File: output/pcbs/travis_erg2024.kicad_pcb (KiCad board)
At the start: 2 copper layers, 406.4 x 146.4 mm, 193 parts

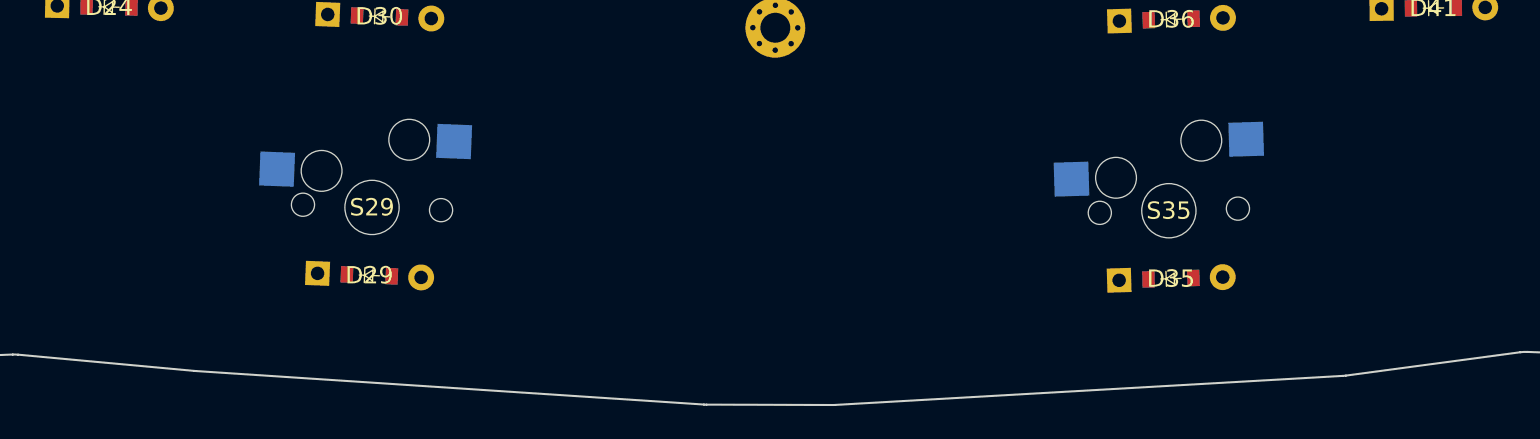
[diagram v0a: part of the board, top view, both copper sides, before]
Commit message: added stabs
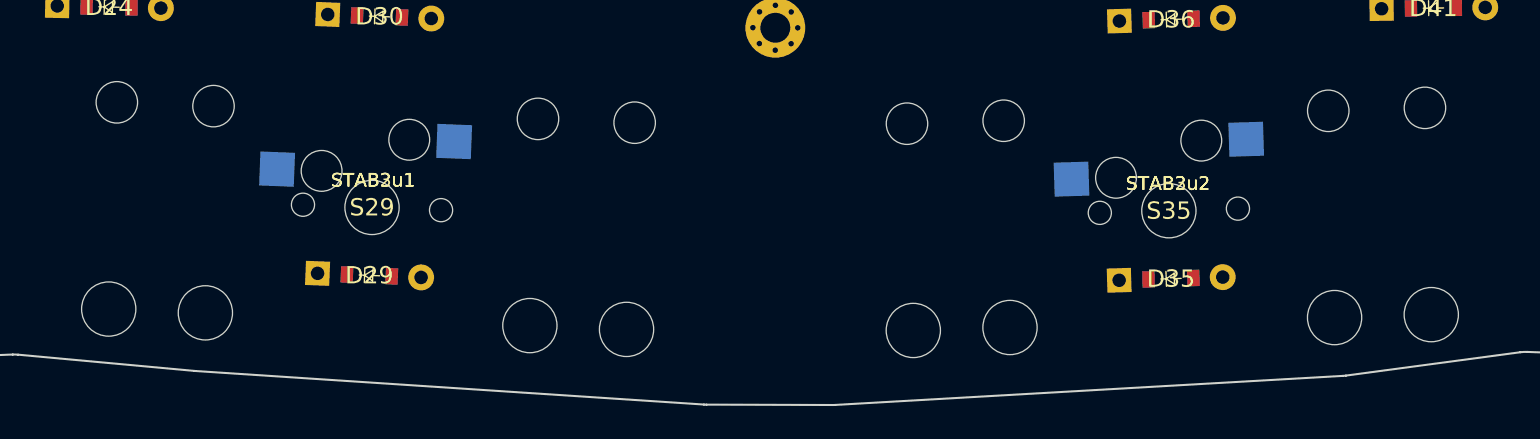
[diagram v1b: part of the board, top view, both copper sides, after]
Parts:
- added STAB2u1: Stabilizer_MX_2.00u, Stabilizer_MX_2.00u, F.Cu at (134.1, 169.9)
- added STAB2u2: Stabilizer_MX_2.00u, Stabilizer_MX_2.00u, F.Cu at (192.7, 170.1)
- added STAB3u1: Stabilizer_MX_3.00u, Stabilizer_MX_3.00u, F.Cu at (134.1, 169.9)
- added STAB3u2: Stabilizer_MX_3.00u, Stabilizer_MX_3.00u, F.Cu at (192.7, 170.1)
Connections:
- DIP1 pad 1: mux0 -> (no net)
- DIP1 pad 10: col5 -> (no net)
- DIP1 pad 11: col4 -> (no net)
- DIP1 pad 12: col3 -> (no net)
- DIP1 pad 13: col2 -> (no net)
- DIP1 pad 14: col1 -> (no net)
- DIP1 pad 15: col0 -> (no net)
- DIP1 pad 2: mux1 -> (no net)
- DIP1 pad 3: mux2 -> (no net)
- DIP1 pad 5: mux3 -> (no net)
- DIP1 pad 7: col7 -> (no net)
- DIP1 pad 9: col6 -> (no net)
- REF** pad D: (no net) -> undefined
- REF** pad S1: GND -> (no net)
- REF** pad S2: GND -> (no net)
- ROT1 pad 1: GND -> (no net)
- ROT1 pad 2: GND -> (no net)

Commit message: try alt stab
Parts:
- STAB2u2: value Stabilizer_MX_2.00u -> MX_Stabilizer_Cutout-2u; footprint Stabilizer_MX_2.00u -> MX_Stabilizer_Cutout-2u
- turned STAB2u1 to 177.75 degrees

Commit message: 3d adjustments
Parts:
- STAB2u2: value MX_Stabilizer_Cutout-2u -> Stabilizer_MX_2.00u; footprint MX_Stabilizer_Cutout-2u -> Stabilizer_MX_2.00u
- turned STAB2u2 to 181.75 degrees
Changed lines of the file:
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@@
     )
   )
-    (module MX_Stabilizer_Cutout-2u (layer F.Cu)
-    (at 192.703245 170.1296884 1.75)
-    (fp_text reference "STAB2u2" (at 0.25 10.05) (layer Eco2.User) hide hide
+    (module Stabilizer_MX_2.00u (layer F.Cu)
+    (descr "MX PCB Stabilizer 2.00u 2.25u 2.50u 2.75u")
+    (tags "MX Keyboard Stabilizer 2.00u 2.25u 2.50u 2.75u Cutout")
+    (at 192.703245 170.1296884 181.75)
+    (attr virtual)
+    (fp_text reference "STAB2u2" (at 0 -2) (layer F.SilkS) hide
       (effects (font (size 1 1) (thickness 0.15)))
     )
-    (fp_text value MX_Stabilizer_Cutout-2u (at 0 -15.24) (layer F.Fab) hide
+    (fp_text value Stabilizer_MX_2.00u (at 0 2) (layer F.Fab)
       (effects (font (size 1 1) (thickness 0.15)))
     )
-    (fp_line (start -19 -9.5) (end 19 -9.5) (layer Dwgs.User) (width 0.15))
-    (fp_line (start -19 9.5) (end -19 -9.5) (layer Dwgs.User) (width 0.15))
-    (fp_line (start 19 9.5) (end -19 9.5) (layer Dwgs.User) (width 0.15))
-    (fp_line (start 19 -9.5) (end 19 9.5) (layer Dwgs.User) (width 0.15))
-    (pad "" np_thru_hole oval (at 11.938 7.7724) (size 3.048 0.3048) (drill oval 3.048 0.3048) (layers *.Cu *.Mask))
-    (pad "" np_thru_hole oval (at 11.938 -5.5372) (size 6.6548 0.3048) (drill oval 6.6548 0.3048) (layers *.Cu *.Mask))
-    (pad "" np_thru_hole oval (at 8.763 0.4572) (size 0.3048 12.2936) (drill oval 0.3048 12.2936) (layers *.Cu *.Mask))
-    (pad "" np_thru_hole oval (at 11.938 6.4516) (size 6.6548 0.3048) (drill oval 6.6548 0.3048) (layers *.Cu *.Mask))
-    (pad "" np_thru_hole oval (at 15.113 0.4572) (size 0.3048 12.2936) (drill oval 0.3048 12.2936) (layers *.Cu *.Mask))
-    (pad "" np_thru_hole oval (at 15.9766 -0.889) (size 0.3048 2.794) (drill oval 0.3048 2.794) (layers *.Cu *.Mask))
-    (pad "" np_thru_hole oval (at 10.5664 7.112) (size 0.3048 1.4732) (drill oval 0.3048 1.4732) (layers *.Cu *.Mask))
-    (pad "" np_thru_hole oval (at 15.5448 -2.1336) (size 1.1684 0.3048) (drill oval 1.1684 0.3048) (layers *.Cu *.Mask))
-    (pad "" np_thru_hole oval (at 13.3096 7.112) (size 0.3048 1.4732) (drill oval 0.3048 1.4732) (layers *.Cu *.Mask))
-    (pad "" np_thru_hole oval (at 15.5448 0.3556) (size 1.1684 0.3048) (drill oval 1.1684 0.3048) (layers *.Cu *.Mask))
-    (pad "" np_thru_hole oval (at -11.938 -5.5372) (size 6.6548 0.3048) (drill oval 6.6548 0.3048) (layers *.Cu *.Mask))
-    (pad "" np_thru_hole oval (at -15.5448 -2.1336) (size 1.1684 0.3048) (drill oval 1.1684 0.3048) (layers *.Cu *.Mask))
-    (pad "" np_thru_hole oval (at -15.9766 -0.889) (size 0.3048 2.794) (drill oval 0.3048 2.794) (layers *.Cu *.Mask))
-    (pad "" np_thru_hole oval (at -15.113 0.4572) (size 0.3048 12.2936) (drill oval 0.3048 12.2936) (layers *.Cu *.Mask))
-    (pad "" np_thru_hole oval (at -8.763 0.4572) (size 0.3048 12.2936) (drill oval 0.3048 12.2936) (layers *.Cu *.Mask))
-    (pad "" np_thru_hole oval (at -11.938 6.4516) (size 6.6548 0.3048) (drill oval 6.6548 0.3048) (layers *.Cu *.Mask))
-    (pad "" np_thru_hole oval (at -15.5448 0.3556) (size 1.1684 0.3048) (drill oval 1.1684 0.3048) (layers *.Cu *.Mask))
-    (pad "" np_thru_hole oval (at -13.3096 7.112) (size 0.3048 1.4732) (drill oval 0.3048 1.4732) (layers *.Cu *.Mask))
-    (pad "" np_thru_hole oval (at -10.5664 7.112) (size 0.3048 1.4732) (drill oval 0.3048 1.4732) (layers *.Cu *.Mask))
-    (pad "" np_thru_hole oval (at -11.938 7.7724) (size 3.048 0.3048) (drill oval 3.048 0.3048) (layers *.Cu *.Mask))
+    (fp_line (start 0 2) (end 0 -2) (layer Dwgs.User) (width 0.1))
+    (fp_line (start -2 0) (end 2 0) (layer Dwgs.User) (width 0.1))
+    (fp_line (start 8.563 -5.53) (end 8.563 6.77) (layer Eco1.User) (width 0.1))
+    (fp_line (start 8.563 6.77) (end 15.313 6.77) (layer Eco1.User) (width 0.1))
+    (fp_line (start 15.313 6.77) (end 15.313 -5.53) (layer Eco1.User) (width 0.1))
+    (fp_line (start 15.313 -5.53) (end 8.563 -5.53) (layer Eco1.User) (width 0.1))
+    (fp_line (start -15.313 -5.53) (end -15.313 6.77) (layer Eco1.User) (width 0.1))
+    (fp_line (start -15.313 6.77) (end -8.563 6.77) (layer Eco1.User) (width 0.1))
+    (fp_line (start -8.563 6.77) (end -8.563 -5.53) (layer Eco1.User) (width 0.1))
+    (fp_line (start -8.563 -5.53) (end -15.313 -5.53) (layer Eco1.User) (width 0.1))
+    (pad "" np_thru_hole circle (at -11.938 -6.985) (size 3.048 3.048) (drill 3.048) (layers *.Cu *.Mask))
+    (pad "" np_thru_hole circle (at 11.938 -6.985) (size 3.048 3.048) (drill 3.048) (layers *.Cu *.Mask))
+    (pad "" np_thru_hole circle (at -11.938 8.225) (size 3.9878 3.9878) (drill 3.9878) (layers *.Cu *.Mask))
+    (pad "" np_thru_hole circle (at 11.938 8.225) (size 3.9878 3.9878) (drill 3.9878) (layers *.Cu *.Mask))
+    (fp_text user %R (at 0 0) (layer F.Fab)
+      (effects (font (size 1 1) (thickness 0.15)))
+    )
+    (model ${SCOTTOKEEBS_KICAD}/3dmodels/ScottoKeebs_Stabilizer.3dshapes/Stabilizer_MX_2.00u.step
+      (at (xyz 0 0 0))
+      (scale (xyz 1 1 1))
+      (rotate (xyz 0 0 0))
+    )
   )
     (module Stabilizer_MX_3.00u (layer F.Cu)

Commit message: hole updates
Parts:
- added HOLE8: , MountingHole_2.2mm_M2_Pad_Via, F.Cu at (317.1, 186.0)
- added HOLE9: , MountingHole_2.2mm_M2_Pad_Via, F.Cu at (25.9, 173.5)
- moved HOLE7 375.8 mm to (398.5, 124.8), turned to 20.25 degrees
- moved HOLE4 275.5 mm to (147.6, 151.4), turned to -2.25 degrees
- moved HOLE5 220.1 mm to (180.0, 151.5), turned to 1.75 degrees
- moved HOLE6 146.5 mm to (412.1, 74.4), turned to -6.25 degrees
- moved HOLE3 64.0 mm to (178.3, 94.3), turned to 1.75 degrees
- moved HOLE2 15.2 mm to (149.8, 94.2), turned to -2.25 degrees
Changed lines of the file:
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@@
     )
     (module "MountingHole_2.2mm_M2_Pad_Via" (version 20210722) (generator pcbnew) (layer "F.Cu")
-      (at 164.0168889 99.56153615 -0.25)
+      (at 149.7979288 94.2448753 -2.25)
       (fp_text reference "HOLE2" (at 0 -3.2) (layer "F.SilkS") hide
         (effects (font (size 1 1) (thickness 0.15)))
@@
     )
     (module "MountingHole_2.2mm_M2_Pad_Via" (version 20210722) (generator pcbnew) (layer "F.Cu")
-      (at 163.76767775 156.67617825 -0.25)
+      (at 178.28185380000002 94.3347446 1.75)
       (fp_text reference "HOLE3" (at 0 -3.2) (layer "F.SilkS") hide
         (effects (font (size 1 1) (thickness 0.15)))
@@
     )
     (module "MountingHole_2.2mm_M2_Pad_Via" (version 20210722) (generator pcbnew) (layer "F.Cu")
-      (at 412.10559179999996 74.38696089999999 -6.25)
+      (at 147.5542304 151.3508147 -2.25)
       (fp_text reference "HOLE4" (at 0 -3.2) (layer "F.SilkS") hide
         (effects (font (size 1 1) (thickness 0.15)))
@@
     )
     (module "MountingHole_2.2mm_M2_Pad_Via" (version 20210722) (generator pcbnew) (layer "F.Cu")
-      (at 398.47511535000007 124.7916516 20.25)
+      (at 180.0271299 151.4580894 1.75)
       (fp_text reference "HOLE5" (at 0 -3.2) (layer "F.SilkS") hide
         (effects (font (size 1 1) (thickness 0.15)))
@@
     )
     (module "MountingHole_2.2mm_M2_Pad_Via" (version 20210722) (generator pcbnew) (layer "F.Cu")
-      (at 317.14183135 185.96621080000003 21.75)
+      (at 412.10559179999996 74.38696089999999 -6.25)
       (fp_text reference "HOLE6" (at 0 -3.2) (layer "F.SilkS") hide
         (effects (font (size 1 1) (thickness 0.15)))
@@
     )
     (module "MountingHole_2.2mm_M2_Pad_Via" (version 20210722) (generator pcbnew) (layer "F.Cu")
-      (at 25.877162499999997 173.46035320000001 2.75)
+      (at 398.47511535000007 124.7916516 20.25)
       (fp_text reference "HOLE7" (at 0 -3.2) (layer "F.SilkS") hide
         (effects (font (size 1 1) (thickness 0.15)))
       )
+      (fp_circle (center 0 0) (end 2.45 0) (layer "F.CrtYd") (width 0.05) (fill none))
+      (pad "1" thru_hole circle locked (at 1.166726 1.166726) (size 0.7 0.7) (drill 0.4) (layers *.Cu *.Mask))
+      (pad "1" thru_hole circle locked (at 0 0) (size 4.4 4.4) (drill 2.2) (layers *.Cu *.Mask))
+      (pad "1" thru_hole circle locked (at 0 1.65) (size 0.7 0.7) (drill 0.4) (layers *.Cu *.Mask))
+      (pad "1" thru_hole circle locked (at 1.166726 -1.166726) (size 0.7 0.7) (drill 0.4) (layers *.Cu *.Mask))
+      (pad "1" thru_hole circle locked (at -1.65 0) (size 0.7 0.7) (drill 0.4) (layers *.Cu *.Mask))
+      (pad "1" thru_hole circle locked (at -1.166726 -1.166726) (size 0.7 0.7) (drill 0.4) (layers *.Cu *.Mask))
+      (pad "1" thru_hole circle locked (at -1.166726 1.166726) (size 0.7 0.7) (drill 0.4) (layers *.Cu *.Mask))
+      (pad "1" thru_hole circle locked (at 1.65 0) (size 0.7 0.7) (drill 0.4) (layers *.Cu *.Mask))
+      (pad "1" thru_hole circle locked (at 0 -1.65) (size 0.7 0.7) (drill 0.4) (layers *.Cu *.Mask))
+    )
+    (module "MountingHole_2.2mm_M2_Pad_Via" (version 20210722) (generator pcbnew) (layer "F.Cu")
+      (at 317.14183135 185.96621080000003 21.75)
+      (fp_text reference "HOLE8" (at 0 -3.2) (layer "F.SilkS") hide
+        (effects (font (size 1 1) (thickness 0.15)))
+      )
+      (fp_circle (center 0 0) (end 2.45 0) (layer "F.CrtYd") (width 0.05) (fill none))
+      (pad "1" thru_hole circle locked (at 1.166726 1.166726) (size 0.7 0.7) (drill 0.4) (layers *.Cu *.Mask))
+      (pad "1" thru_hole circle locked (at 0 0) (size 4.4 4.4) (drill 2.2) (layers *.Cu *.Mask))
+      (pad "1" thru_hole circle locked (at 0 1.65) (size 0.7 0.7) (drill 0.4) (layers *.Cu *.Mask))
+      (pad "1" thru_hole circle locked (at 1.166726 -1.166726) (size 0.7 0.7) (drill 0.4) (layers *.Cu *.Mask))
+      (pad "1" thru_hole circle locked (at -1.65 0) (size 0.7 0.7) (drill 0.4) (layers *.Cu *.Mask))
+      (pad "1" thru_hole circle locked (at -1.166726 -1.166726) (size 0.7 0.7) (drill 0.4) (layers *.Cu *.Mask))
+      (pad "1" thru_hole circle locked (at -1.166726 1.166726) (size 0.7 0.7) (drill 0.4) (layers *.Cu *.Mask))
+      (pad "1" thru_hole circle locked (at 1.65 0) (size 0.7 0.7) (drill 0.4) (layers *.Cu *.Mask))
+      (pad "1" thru_hole circle locked (at 0 -1.65) (size 0.7 0.7) (drill 0.4) (layers *.Cu *.Mask))
+    )
+    (module "MountingHole_2.2mm_M2_Pad_Via" (version 20210722) (generator pcbnew) (layer "F.Cu")
+      (at 25.877162499999997 173.46035320000001 2.75)
+      (fp_text reference "HOLE9" (at 0 -3.2) (layer "F.SilkS") hide
+        (effects (font (size 1 1) (thickness 0.15)))
+      )

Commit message: tweak splay
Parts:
- moved HOLE6 22.1 mm to (392.1, 64.8), turned to -0.334 degrees
- moved S88 20.5 mm to (384.5, 78.3), turned to -0.334 degrees
- moved D88 20.1 mm to (384.5, 83.3), turned to -0.334 degrees
- moved S86 19.9 mm to (365.5, 78.2), turned to -0.334 degrees
- moved B1 19.5 mm to (351.2, 78.1), turned to -45.334 degrees
- moved D86 19.4 mm to (365.5, 83.2), turned to -0.334 degrees
- moved S76 19.3 mm to (336.9, 78.0), turned to -0.334 degrees
- moved D76 18.8 mm to (336.9, 83.0), turned to -0.334 degrees
- moved S87 18.7 mm to (384.4, 97.4), turned to -0.334 degrees
- moved D87 18.3 mm to (384.4, 102.4), turned to -0.334 degrees
- moved S85 18.0 mm to (365.4, 97.3), turned to -0.334 degrees
- moved D85 17.5 mm to (365.3, 102.3), turned to -0.334 degrees
- moved S75 17.4 mm to (317.9, 77.9), turned to -0.334 degrees
- moved D75 17.0 mm to (317.8, 82.9), turned to -0.334 degrees
- moved S74 15.8 mm to (323.1, 97.0), turned to -0.334 degrees
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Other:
- board size 406.4 x 146.4 mm -> 393 x 144.9 mm

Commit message: tweak rotation, position
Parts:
- moved D52 8.00 mm to (249.1, 176.0)
- moved D62 8.00 mm to (268.6, 101.6)
- moved D82 8.00 mm to (356.1, 141.9)
- moved S52 8.00 mm to (249.1, 171.0)
- moved S62 8.00 mm to (268.6, 96.6)
- moved S82 8.00 mm to (352.4, 138.6)
- moved D58 8.00 mm to (268.1, 177.8)
- moved D69 8.00 mm to (311.8, 139.9)
- moved D76 8.00 mm to (344.9, 83.0)
- moved D85 8.00 mm to (373.3, 102.2)
- moved S58 8.00 mm to (268.2, 172.8)
- moved S69 8.00 mm to (311.8, 134.9)
- moved S76 8.00 mm to (344.9, 78.0)
- moved S85 8.00 mm to (373.4, 97.2)
- moved D13 8.00 mm to (75.2, 158.1)
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
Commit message: updated plate
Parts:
- moved D3 1.00 mm to (32.4, 141.5)
- moved D53 1.00 mm to (249.9, 156.9)
- moved D65 1.00 mm to (288.4, 139.8)
- moved D72 1.00 mm to (307.8, 82.7)
- moved D8 1.00 mm to (56.9, 160.3)
- moved D81 1.00 mm to (371.2, 154.7)
- moved D88 1.00 mm to (393.5, 83.2)
- moved HOLE6 1.00 mm to (401.1, 64.7)
- moved S3 1.00 mm to (32.3, 136.5)
- moved S53 1.00 mm to (249.9, 151.9)
- moved S65 1.00 mm to (288.4, 134.8)
- moved S72 1.00 mm to (307.8, 77.7)
- moved S8 1.00 mm to (56.9, 155.3)
- moved S81 1.00 mm to (367.5, 151.4)
- moved S88 1.00 mm to (393.5, 78.2)
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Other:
- board size 393 x 144.9 mm -> 393 x 145.1 mm

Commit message: added rgb leds, moved diodes
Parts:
- added LED1: , ceoloide:led_SK6812mini-e (per-keysingle-side), B.Cu at (38.1, 179.5)
- added LED10: , ceoloide:led_SK6812mini-e (per-keysingle-side), B.Cu at (56.5, 122.2)
- added LED11: , ceoloide:led_SK6812mini-e (per-keysingle-side), B.Cu at (56.3, 103.1)
- added LED12: , ceoloide:led_SK6812mini-e (per-keysingle-side), B.Cu at (76.1, 177.1)
- added LED13: , ceoloide:led_SK6812mini-e (per-keysingle-side), B.Cu at (76.2, 158.0)
- added LED14: , ceoloide:led_SK6812mini-e (per-keysingle-side), B.Cu at (76.3, 139.0)
- added LED15: , ceoloide:led_SK6812mini-e (per-keysingle-side), B.Cu at (76.4, 119.9)
- added LED16: , ceoloide:led_SK6812mini-e (per-keysingle-side), B.Cu at (76.5, 100.9)
- added LED17: , ceoloide:led_SK6812mini-e (per-keysingle-side), B.Cu at (76.6, 81.8)
- added LED18: , ceoloide:led_SK6812mini-e (per-keysingle-side), B.Cu at (95.0, 176.2)
- added LED19: , ceoloide:led_SK6812mini-e (per-keysingle-side), B.Cu at (95.5, 157.2)
- added LED2: , ceoloide:led_SK6812mini-e (per-keysingle-side), B.Cu at (32.6, 160.5)
- added LED20: , ceoloide:led_SK6812mini-e (per-keysingle-side), B.Cu at (95.9, 138.1)
- added LED21: , ceoloide:led_SK6812mini-e (per-keysingle-side), B.Cu at (96.4, 119.1)
- added LED22: , ceoloide:led_SK6812mini-e (per-keysingle-side), B.Cu at (96.8, 100.0)
- added LED23: , ceoloide:led_SK6812mini-e (per-keysingle-side), B.Cu at (97.3, 81.0)
- added LED24: , ceoloide:led_SK6812mini-e (per-keysingle-side), B.Cu at (114.8, 158.6)
- added LED25: , ceoloide:led_SK6812mini-e (per-keysingle-side), B.Cu at (115.5, 139.6)
- added LED26: , ceoloide:led_SK6812mini-e (per-keysingle-side), B.Cu at (116.3, 120.5)
- added LED27: , ceoloide:led_SK6812mini-e (per-keysingle-side), B.Cu at (117.1, 101.5)
- added LED28: , ceoloide:led_SK6812mini-e (per-keysingle-side), B.Cu at (117.9, 82.5)
- added LED29: , ceoloide:led_SK6812mini-e (per-keysingle-side), B.Cu at (133.6, 178.7)
- added LED3: , ceoloide:led_SK6812mini-e (per-keysingle-side), B.Cu at (32.4, 141.5)
- added LED30: , ceoloide:led_SK6812mini-e (per-keysingle-side), B.Cu at (134.4, 159.7)
- added LED31: , ceoloide:led_SK6812mini-e (per-keysingle-side), B.Cu at (135.2, 140.6)
- added LED32: , ceoloide:led_SK6812mini-e (per-keysingle-side), B.Cu at (135.9, 121.6)
- added LED33: , ceoloide:led_SK6812mini-e (per-keysingle-side), B.Cu at (136.7, 102.6)
- added LED34: , ceoloide:led_SK6812mini-e (per-keysingle-side), B.Cu at (137.5, 83.5)
- added LED35: , ceoloide:led_SK6812mini-e (per-keysingle-side), B.Cu at (192.6, 178.5)
- added LED36: , ceoloide:led_SK6812mini-e (per-keysingle-side), B.Cu at (192.4, 159.5)
- added LED37: , ceoloide:led_SK6812mini-e (per-keysingle-side), B.Cu at (191.5, 140.4)
- added LED38: , ceoloide:led_SK6812mini-e (per-keysingle-side), B.Cu at (190.6, 121.4)
- added LED39: , ceoloide:led_SK6812mini-e (per-keysingle-side), B.Cu at (189.7, 102.4)
- added LED4: , ceoloide:led_SK6812mini-e (per-keysingle-side), B.Cu at (32.2, 122.4)
- added LED40: , ceoloide:led_SK6812mini-e (per-keysingle-side), B.Cu at (188.8, 83.4)
- added LED41: , ceoloide:led_SK6812mini-e (per-keysingle-side), B.Cu at (211.4, 158.3)
- added LED42: , ceoloide:led_SK6812mini-e (per-keysingle-side), B.Cu at (210.5, 139.3)
- added LED43: , ceoloide:led_SK6812mini-e (per-keysingle-side), B.Cu at (209.6, 120.3)
- added LED44: , ceoloide:led_SK6812mini-e (per-keysingle-side), B.Cu at (208.7, 101.2)
- added LED45: , ceoloide:led_SK6812mini-e (per-keysingle-side), B.Cu at (207.8, 82.2)
- added LED46: , ceoloide:led_SK6812mini-e (per-keysingle-side), B.Cu at (231.2, 175.5)
- added LED47: , ceoloide:led_SK6812mini-e (per-keysingle-side), B.Cu at (230.6, 156.4)
- added LED48: , ceoloide:led_SK6812mini-e (per-keysingle-side), B.Cu at (230.1, 137.4)
- added LED49: , ceoloide:led_SK6812mini-e (per-keysingle-side), B.Cu at (229.5, 118.4)
- added LED5: , ceoloide:led_SK6812mini-e (per-keysingle-side), B.Cu at (37.2, 103.3)
- added LED50: , ceoloide:led_SK6812mini-e (per-keysingle-side), B.Cu at (228.9, 99.3)
- added LED51: , ceoloide:led_SK6812mini-e (per-keysingle-side), B.Cu at (228.4, 80.3)
- added LED52: , ceoloide:led_SK6812mini-e (per-keysingle-side), B.Cu at (250.1, 175.9)
- added LED53: , ceoloide:led_SK6812mini-e (per-keysingle-side), B.Cu at (249.9, 156.9)
- added LED54: , ceoloide:led_SK6812mini-e (per-keysingle-side), B.Cu at (249.7, 137.8)
- added LED55: , ceoloide:led_SK6812mini-e (per-keysingle-side), B.Cu at (249.5, 118.8)
- added LED56: , ceoloide:led_SK6812mini-e (per-keysingle-side), B.Cu at (249.3, 99.7)
- added LED57: , ceoloide:led_SK6812mini-e (per-keysingle-side), B.Cu at (249.0, 80.7)
- added LED58: , ceoloide:led_SK6812mini-e (per-keysingle-side), B.Cu at (269.1, 177.7)
- added LED59: , ceoloide:led_SK6812mini-e (per-keysingle-side), B.Cu at (269.2, 158.7)
- added LED6: , ceoloide:led_SK6812mini-e (per-keysingle-side), B.Cu at (37.0, 84.3)
- added LED60: , ceoloide:led_SK6812mini-e (per-keysingle-side), B.Cu at (269.4, 139.6)
- added LED61: , ceoloide:led_SK6812mini-e (per-keysingle-side), B.Cu at (269.5, 120.6)
- added LED62: , ceoloide:led_SK6812mini-e (per-keysingle-side), B.Cu at (269.6, 101.5)
- added LED63: , ceoloide:led_SK6812mini-e (per-keysingle-side), B.Cu at (288.2, 177.8)
- added LED64: , ceoloide:led_SK6812mini-e (per-keysingle-side), B.Cu at (293.7, 158.8)
- added LED65: , ceoloide:led_SK6812mini-e (per-keysingle-side), B.Cu at (288.4, 139.7)
- added LED66: , ceoloide:led_SK6812mini-e (per-keysingle-side), B.Cu at (288.5, 120.7)
- added LED67: , ceoloide:led_SK6812mini-e (per-keysingle-side), B.Cu at (288.6, 101.6)
- added LED68: , ceoloide:led_SK6812mini-e (per-keysingle-side), B.Cu at (288.7, 82.6)
- added LED69: , ceoloide:led_SK6812mini-e (per-keysingle-side), B.Cu at (312.8, 139.9)
- added LED7: , ceoloide:led_SK6812mini-e (per-keysingle-side), B.Cu at (57.1, 179.3)
- added LED70: , ceoloide:led_SK6812mini-e (per-keysingle-side), B.Cu at (307.6, 120.8)
- added LED71: , ceoloide:led_SK6812mini-e (per-keysingle-side), B.Cu at (307.7, 101.7)
- added LED72: , ceoloide:led_SK6812mini-e (per-keysingle-side), B.Cu at (307.8, 82.7)
- added LED73: , ceoloide:led_SK6812mini-e (per-keysingle-side), B.Cu at (326.6, 120.9)
- added LED74: , ceoloide:led_SK6812mini-e (per-keysingle-side), B.Cu at (332.1, 101.9)
- added LED75: , ceoloide:led_SK6812mini-e (per-keysingle-side), B.Cu at (326.8, 82.8)
- added LED76: , ceoloide:led_SK6812mini-e (per-keysingle-side), B.Cu at (345.9, 82.9)
- added LED77: , ceoloide:led_SK6812mini-e (per-keysingle-side), B.Cu at (342.3, 186.4)
- added LED78: , ceoloide:led_SK6812mini-e (per-keysingle-side), B.Cu at (328.2, 173.6)
- added LED79: , ceoloide:led_SK6812mini-e (per-keysingle-side), B.Cu at (355.1, 172.3)
- added LED8: , ceoloide:led_SK6812mini-e (per-keysingle-side), B.Cu at (56.9, 160.3)
- added LED80: , ceoloide:led_SK6812mini-e (per-keysingle-side), B.Cu at (341.1, 159.5)
- added LED81: , ceoloide:led_SK6812mini-e (per-keysingle-side), B.Cu at (371.2, 154.7)
- added LED82: , ceoloide:led_SK6812mini-e (per-keysingle-side), B.Cu at (357.1, 141.9)
- added LED83: , ceoloide:led_SK6812mini-e (per-keysingle-side), B.Cu at (384.0, 140.6)
- added LED84: , ceoloide:led_SK6812mini-e (per-keysingle-side), B.Cu at (369.9, 127.8)
- added LED85: , ceoloide:led_SK6812mini-e (per-keysingle-side), B.Cu at (374.3, 102.1)
- added LED86: , ceoloide:led_SK6812mini-e (per-keysingle-side), B.Cu at (374.5, 83.1)
- added LED87: , ceoloide:led_SK6812mini-e (per-keysingle-side), B.Cu at (393.4, 102.2)
- added LED88: , ceoloide:led_SK6812mini-e (per-keysingle-side), B.Cu at (393.5, 83.2)
- added LED9: , ceoloide:led_SK6812mini-e (per-keysingle-side), B.Cu at (56.7, 141.2)
- moved D35 8.16 mm to (199.7, 174.5), turned to 92.666 degrees
- moved D36 8.16 mm to (199.4, 155.4), turned to 92.666 degrees
- moved D37 8.16 mm to (198.5, 136.4), turned to 92.666 degrees
- moved D38 8.16 mm to (197.7, 117.4), turned to 92.666 degrees
- moved D39 8.16 mm to (196.8, 98.3), turned to 92.666 degrees
- moved D40 8.16 mm to (195.9, 79.3), turned to 92.666 degrees
- moved D41 8.16 mm to (218.4, 154.3), turned to 92.666 degrees
- moved D42 8.16 mm to (217.6, 135.3), turned to 92.666 degrees
- moved D43 8.16 mm to (216.7, 116.2), turned to 92.666 degrees
- moved D44 8.16 mm to (215.8, 97.2), turned to 92.666 degrees
- moved D45 8.16 mm to (214.9, 78.2), turned to 92.666 degrees
- moved D46 8.16 mm to (238.3, 171.6), turned to 91.666 degrees
- moved D47 8.16 mm to (237.7, 152.5), turned to 91.666 degrees
- moved D48 8.16 mm to (237.2, 133.5), turned to 91.666 degrees
- moved D49 8.16 mm to (236.6, 114.4), turned to 91.666 degrees
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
